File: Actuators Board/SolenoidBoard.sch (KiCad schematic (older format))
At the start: 27 parts, among them J10 Conn_01x02_Male, J9 Conn_01x02_Male, Q1 MMDT2222A

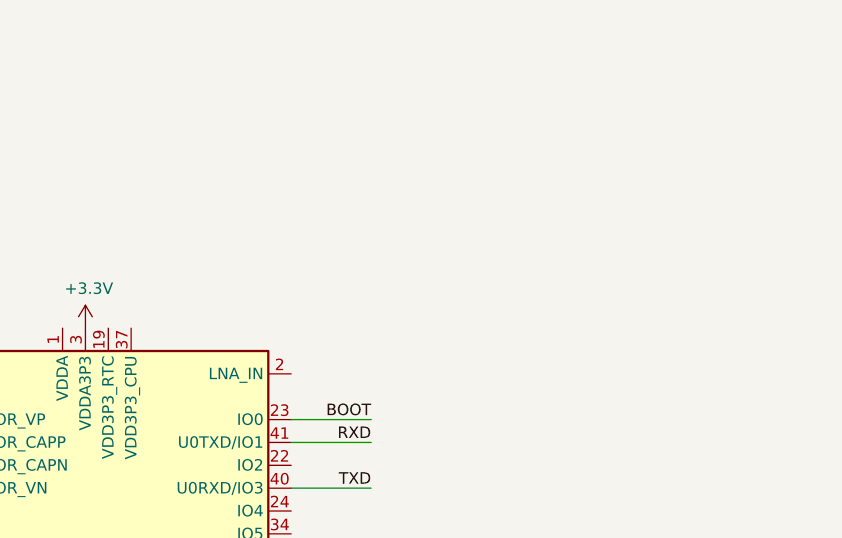
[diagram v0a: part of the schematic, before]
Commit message: Added Rf antenna to all boards
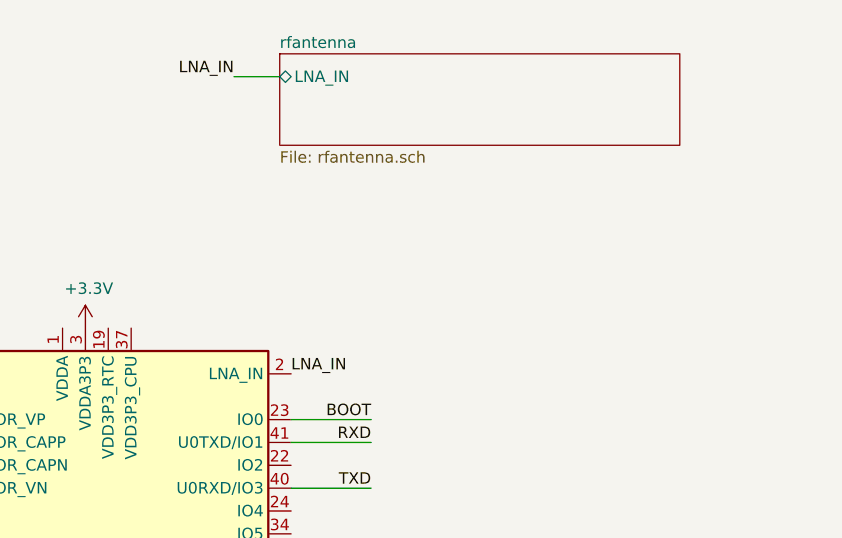
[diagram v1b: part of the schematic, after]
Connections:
- net LNA_IN: now reaches U?.2 (LNA_IN)
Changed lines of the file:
@@
 $Descr A4 11693 8268
 encoding utf-8
-Sheet 1 3
+Sheet 1 4
 Title ""
 Date ""
@@
 F1 "can.sch" 50
 $EndSheet
+Text Label 5000 2150 0    50   ~ 0
+LNA_IN
+$Sheet
+S 4950 750  1750 400
+U 61A49DAE
+F0 "rfantenna" 50
+F1 "rfantenna.sch" 50
+F2 "LNA_IN" B L 4950 850 50
+$EndSheet
+Wire Wire Line
+	4950 850  4750 850
+Text Label 4750 850  2    50   ~ 0
+LNA_IN
 $EndSCHEMATC
